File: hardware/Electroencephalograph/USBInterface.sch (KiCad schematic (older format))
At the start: 33 parts, among them J5 USB_B_Micro, J7 Conn_01x04_Female, Q1 FDV304P, Q2 FDV304P, Q3 FDV304P, U12 ESP-12E, U6 FT200XD

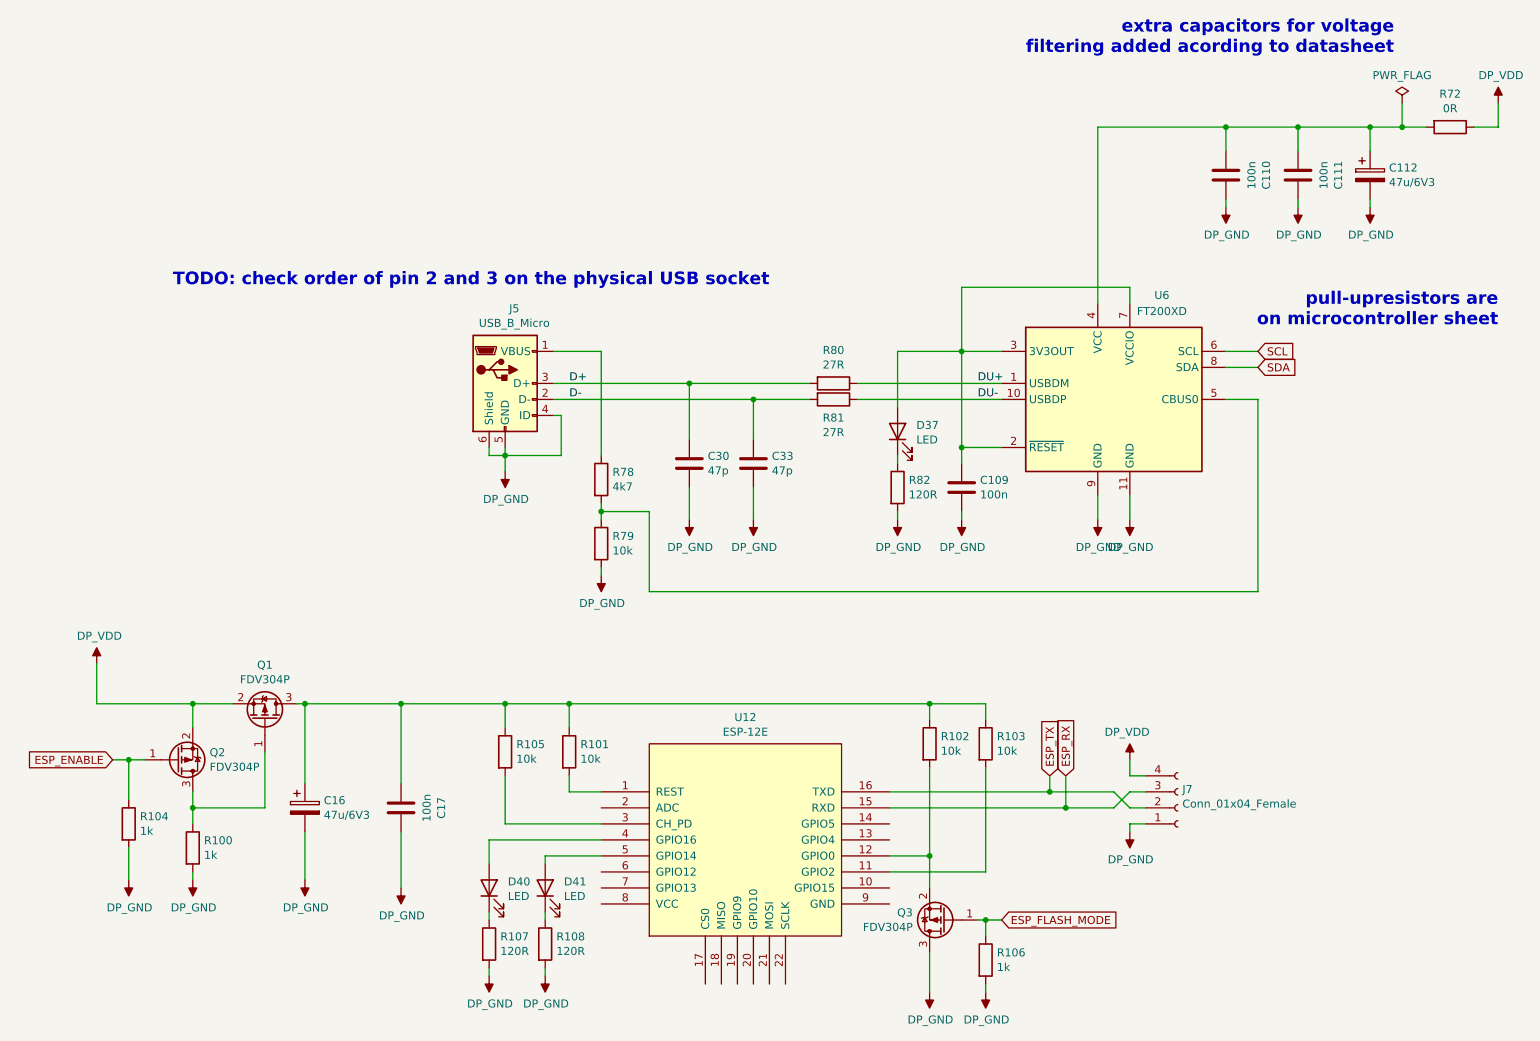
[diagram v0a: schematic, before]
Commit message: split user interface to separate sheets
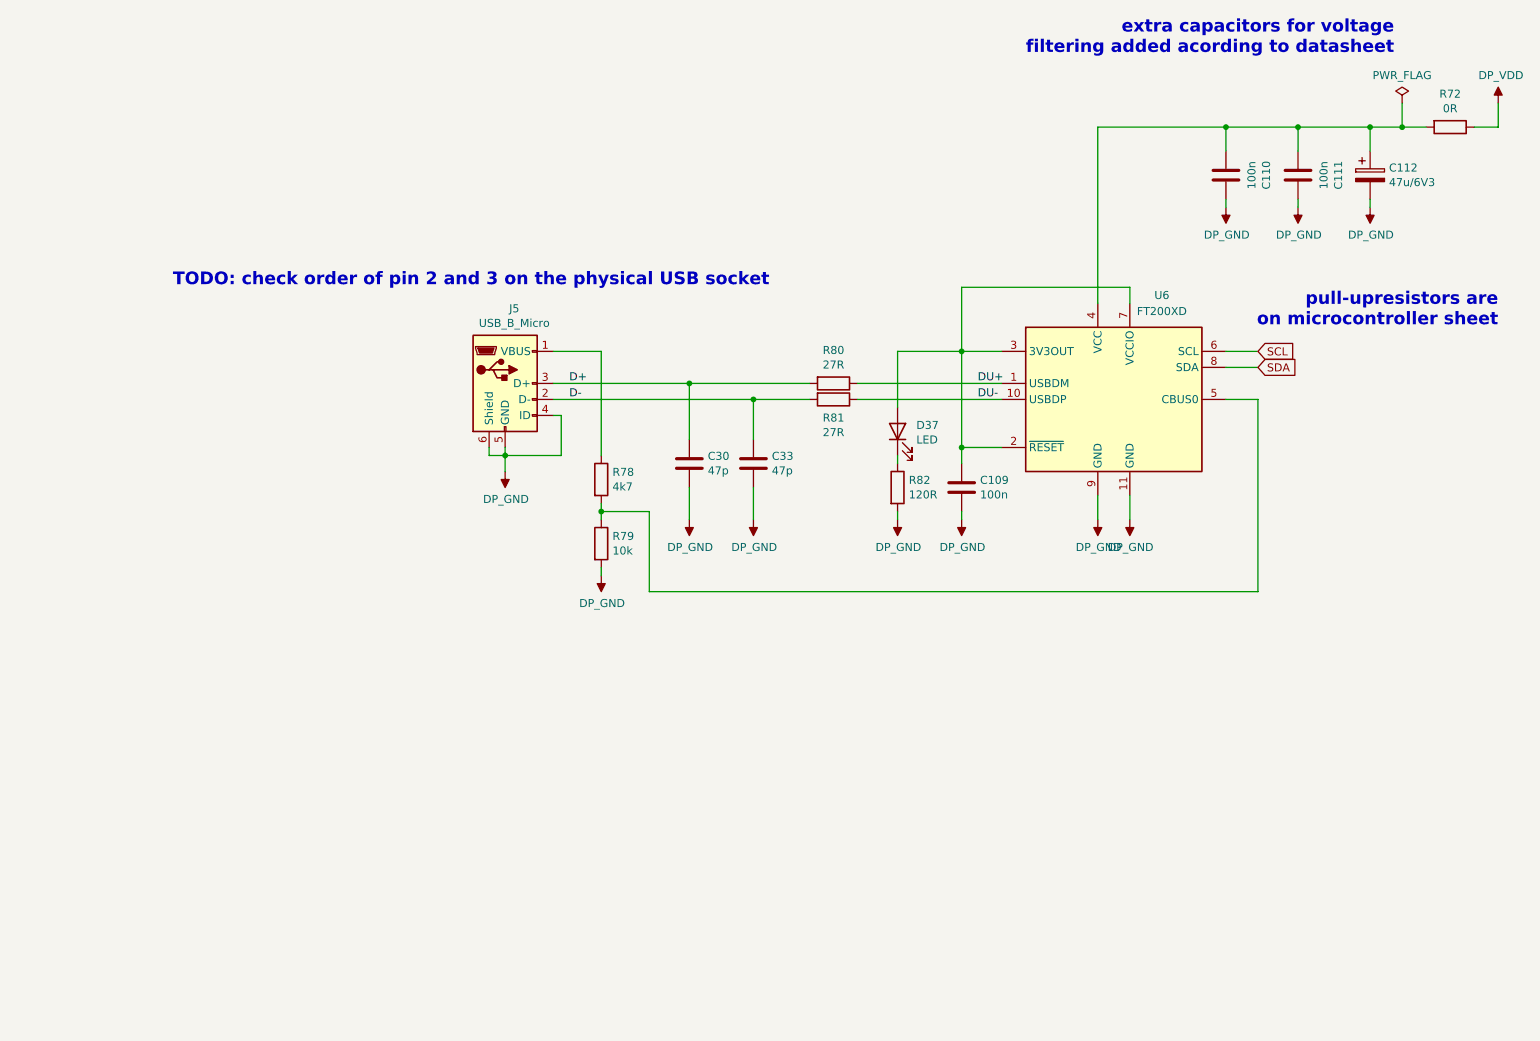
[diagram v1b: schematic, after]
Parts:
- removed C16: 47u/6V3, Capacitor_Tantalum_SMD:CP_EIA-3528-21_Kemet-B, symbol Device:CP
- removed C17: 100n, Capacitor_SMD:C_0402_1005Metric, symbol Device:C
- removed D40, D41: LED, LED_SMD:LED_0402_1005Metric, symbol Device:LED
- removed J7: Conn_01x04_Female, Connector_PinHeader_2.54mm:PinHeader_1x04_P2.54mm_Vertical, symbol Connector:Conn_01x04_Female
- removed Q1, Q2, Q3: FDV304P, Package_TO_SOT_SMD:SOT-23, symbol Device:Q_PMOS_GSD
- removed R100, R104, R106: 1k, Resistor_SMD:R_0402_1005Metric, symbol Device:R
- removed R101, R102, R103, R105: 10k, Resistor_SMD:R_0402_1005Metric, symbol Device:R
- removed R107, R108: 120R, Resistor_SMD:R_0402_1005Metric, symbol Device:R
- removed U12: ESP-12E, ESP8266:ESP-12E, symbol ESP8266:ESP-12E

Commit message: further routing of mcu part
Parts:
- removed R72: 0R, Resistor_SMD:R_0402_1005Metric, symbol Device:R
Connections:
- net DP_VDD: now also C110.1, C111.1, C112.1, U6.4 (VCC)
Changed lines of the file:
@@
 	8150 1500 8600 1500
 Connection ~ 8150 1500
-$Comp
-L Device:R R?
-U 1 1 5ED1AA8A
-P 9100 1500
-AR Path="/5DD5C7F6/5ED1AA8A" Ref="R?"  Part="1"
-AR Path="/5DD5CD1D/5ED1AA8A" Ref="R?"  Part="1"
-AR Path="/5E27E78E/5ED1AA8A" Ref="R72"  Part="1"
-F 0 "R72" V 8893 1500 50  0000 C CNN
-F 1 "0R" V 8984 1500 50  0000 C CNN
-F 2 "Resistor_SMD:R_0402_1005Metric" V 9030 1500 50  0001 C CNN
-F 3 "~" H 9100 1500 50  0001 C CNN
-	1    9100 1500
-	0    1    1    0
-$EndComp
-Wire Wire Line
-	8600 1500 8800 1500
 Connection ~ 8600 1500
 Wire Wire Line
-	9250 1500 9400 1500
-$Comp
-L power:PWR_FLAG #FLG02
-U 1 1 5ED1FF8B
-P 8800 1350
-F 0 "#FLG02" H 8800 1425 50  0001 C CNN
-F 1 "PWR_FLAG" H 8800 1523 50  0000 C CNN
-F 2 "" H 8800 1350 50  0001 C CNN
-F 3 "~" H 8800 1350 50  0001 C CNN
-	1    8800 1350
-	1    0    0    -1
-$EndComp
-Wire Wire Line
-	8800 1350 8800 1500
-Connection ~ 8800 1500
-Wire Wire Line
-	8800 1500 8950 1500
+	8600 1500 9400 1500
 $EndSCHEMATC
